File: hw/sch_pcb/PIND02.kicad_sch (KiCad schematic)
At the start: 56 parts, among them J1 Conn_Coaxial, J2 HEADER_2x05_PARALLEL, J3 HEADER_2x01, M1 HOLE M3, M2 HOLE M3, M3 HOLE, M4 HOLE, Q1 2SK2394-6, U1 OPA2314, U3 ISL21080DIH312Z-TK, U3 SHT31-DIS, U4 TPS613222ADBV

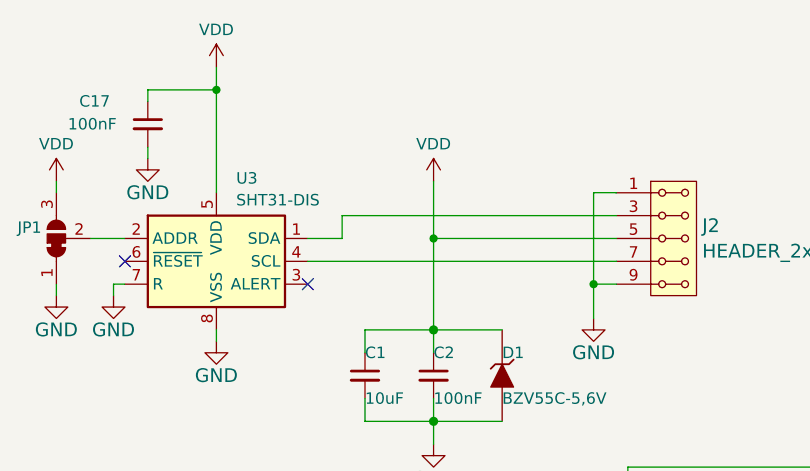
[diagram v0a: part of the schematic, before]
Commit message: Update title block Resolve ERC errors.
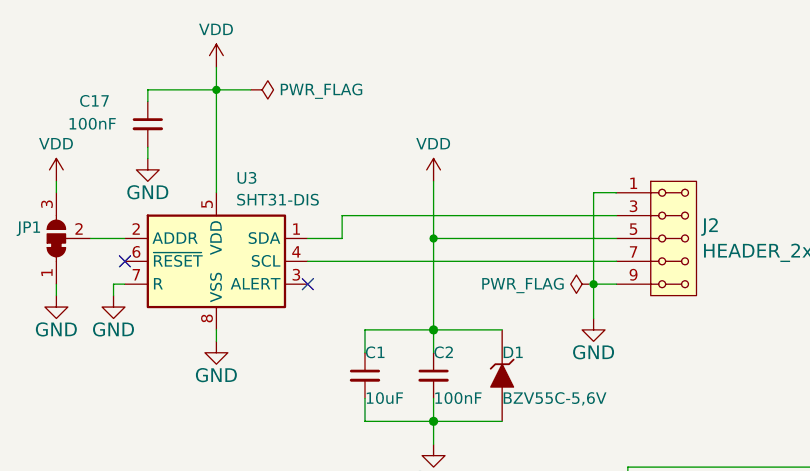
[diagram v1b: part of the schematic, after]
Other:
- company: Mlab www.mlab.cz -> kaklik@mlab.cz
- title: NAME -> PIND02A
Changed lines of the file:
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@@
   (paper "A4")
   (title_block
-    (title "NAME")
+    (title "PIND02A")
     (date "%d. %m. %Y")
-    (rev "REV")
-    (company "Mlab www.mlab.cz")
-    (comment 1 "Short description \\nTwo lines are maximum")
-    (comment 2 "nickname <email@example.com>")
+    (rev "A")
+    (company "kaklik@mlab.cz")
+    (comment 1 "PIN diode semiconductor radiation \\ndetector analogue front-end. ")
   )
   (junction (at 66.04 49.53) (diameter 1.016) (color 0 0 0 0)
@@
     (stroke (width 0) (type default))
   )
+  (wire (pts (xy 41.91 22.86) (xy 45.72 22.86))
+    (stroke (width 0) (type default))
+  )
   (wire (pts (xy 198.12 130.81) (xy 205.74 130.81))
     (stroke (width 0) (type solid))
@@
     )
   )
+  (symbol (lib_id "power:PWR_FLAG") (at 83.82 44.45 90) (unit 1)
+    (in_bom yes) (on_board yes) (dnp no) (fields_autoplaced)
+    (property "Reference" "#FLG03" (at 81.915 44.45 0)
+      (effects (font (size 1.27 1.27)) hide)
+    )
+    (property "Value" "PWR_FLAG" (at 80.6451 44.45 90)
+      (effects (font (size 1.27 1.27)) (justify left))
+    )
+    (property "Footprint" "" (at 83.82 44.45 0)
+      (effects (font (size 1.27 1.27)) hide)
+    )
+    (property "Datasheet" "~" (at 83.82 44.45 0)
+      (effects (font (size 1.27 1.27)) hide)
+    )
+    (pin "1")
+    (instances
+      (project "PIND02"
+        (path "/2ae32537-a16f-4c5b-a56b-c6dddfb8ddb4"
+          (reference "#FLG03") (unit 1)
+        )
+      )
+    )
+  )
   (symbol (lib_id "power:VDD") (at 41.91 20.32 0) (unit 1)
     (in_bom yes) (on_board yes) (dnp no) (fields_autoplaced)
@@
         )
       )
+    )
+  )
+  (symbol (lib_id "power:PWR_FLAG") (at 45.72 22.86 270) (unit 1)
+    (in_bom yes) (on_board yes) (dnp no) (fields_autoplaced)
+    (property "Reference" "#FLG02" (at 47.625 22.86 0)
+      (effects (font (size 1.27 1.27)) hide)
+    )
+    (property "Value" "PWR_FLAG" (at 48.895 22.86 90)
+      (effects (font (size 1.27 1.27)) (justify left))
+    )
+    (property "Footprint" "" (at 45.72 22.86 0)
+      (effects (font (size 1.27 1.27)) hide)
+    )
+    (property "Datasheet" "~" (at 45.72 22.86 0)
+      (effects (font (size 1.27 1.27)) hide)
+    )
+    (pin "1")
+    (instances
+      (project "PIND02"
+        (path "/2ae32537-a16f-4c5b-a56b-c6dddfb8ddb4"
+          (reference "#FLG02") (unit 1)
+        )
+      )

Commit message: Assing footprints to components. Starting of PCB design.
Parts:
- FID1, FID2: footprint (none) -> Fiducial:Fiducial_1mm_Mask2mm
- J1: footprint (none) -> Connector_Coaxial:SMA_Amphenol_901-144_Vertical; UST_ID (none) -> 5fa10cc512875025b39779f6
- J2: footprint (none) -> Mlab_Pin_Headers:Straight_2x05
- J3: footprint (none) -> Mlab_Pin_Headers:Straight_2x01
- JP1: footprint (none) -> Jumper:SolderJumper-3_P1.3mm_Bridged12_RoundedPad1.0x1.5mm
- L3: footprint (none) -> Inductor_SMD:L_0805_2012Metric; UST_ID (none) -> 626fd6fcdc56076e9a222966
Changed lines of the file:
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@@
       (effects (font (size 1.27 1.27)) (justify left))
     )
-    (property "Footprint" "" (at 24.13 39.37 0)
+    (property "Footprint" "Jumper:SolderJumper-3_P1.3mm_Bridged12_RoundedPad1.0x1.5mm" (at 24.13 39.37 0)
       (effects (font (size 1.27 1.27)) hide)
     )
     (property "Datasheet" "~" (at 24.13 39.37 0)
+      (effects (font (size 1.27 1.27)) hide)
+    )
+    (property "UST_ID" "" (at 24.13 39.37 0)
       (effects (font (size 1.27 1.27)) hide)
     )
@@
       (effects (font (size 1.27 1.27)) (justify left))
     )
-    (property "Footprint" "" (at 210.82 130.81 0)
+    (property "Footprint" "Connector_Coaxial:SMA_Amphenol_901-144_Vertical" (at 210.82 130.81 0)
       (effects (font (size 1.27 1.27)) hide)
     )
     (property "Datasheet" " ~" (at 210.82 130.81 0)
+      (effects (font (size 1.27 1.27)) hide)
+    )
+    (property "UST_ID" "5fa10cc512875025b39779f6" (at 210.82 130.81 0)
       (effects (font (size 1.27 1.27)) hide)
     )
@@
       (effects (font (size 1.524 1.524)) (justify left))
     )
-    (property "Footprint" "" (at 198.12 101.6 0)
-      (effects (font (size 1.524 1.524)))
+    (property "Footprint" "Mlab_Pin_Headers:Straight_2x01" (at 198.12 101.6 0)
+      (effects (font (size 1.524 1.524)) hide)
     )
     (property "Datasheet" "" (at 198.12 101.6 0)
       (effects (font (size 1.524 1.524)))
+    )
+    (property "UST_ID" "" (at 198.12 101.6 0)
+      (effects (font (size 1.27 1.27)) hide)
     )
     (pin "1")
@@
       (effects (font (size 1.27 1.27)) (justify left))
     )
-    (property "Footprint" "" (at 271.78 33.02 0)
+    (property "Footprint" "Fiducial:Fiducial_1mm_Mask2mm" (at 271.78 33.02 0)
       (effects (font (size 1.27 1.27)) hide)
     )
@@
       (effects (font (size 1.27 1.27)) (justify left))
     )
-    (property "Footprint" "" (at 259.08 33.02 0)
+    (property "Footprint" "Fiducial:Fiducial_1mm_Mask2mm" (at 259.08 33.02 0)
       (effects (font (size 1.27 1.27)) hide)
     )
@@
       (effects (font (size 1.27 1.27)) (justify left))
     )
-    (property "Footprint" "" (at 198.12 123.19 0)
-      (effects (font (size 1.27 1.27)) hide)
-    )
-    (property "Datasheet" "~" (at 198.12 123.19 0)
+    (property "Footprint" "Inductor_SMD:L_0805_2012Metric" (at 198.12 123.19 0)
+      (effects (font (size 1.27 1.27)) hide)
+    )
+    (property "Datasheet" "https://www.tme.eu/Document/a05ae3504cfc60ed89e3a57fb94acf5e/VIKING-NL.pdf" (at 198.12 123.19 0)
+      (effects (font (size 1.27 1.27)) hide)
+    )
+    (property "UST_ID" "626fd6fcdc56076e9a222966" (at 198.12 123.19 0)
       (effects (font (size 1.27 1.27)) hide)
     )
@@
       (effects (font (size 1.524 1.524)) (justify left))
     )
-    (property "Footprint" "" (at 92.71 34.29 0)
-      (effects (font (size 1.524 1.524)))
+    (property "Footprint" "Mlab_Pin_Headers:Straight_2x05" (at 92.71 34.29 0)
+      (effects (font (size 1.524 1.524)) hide)
     )
     (property "Datasheet" "" (at 92.71 34.29 0)

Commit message: PCB design WIP.
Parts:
- removed C11, C21, C23, C53: 10uF, Capacitor_SMD:C_0603_1608Metric, symbol Device:C
- removed C42, C50: 10uF, Capacitor_SMD:C_0603_1608Metric, symbol SPACEDOS01A_PCB01A-rescue:C-device-DATALOGGER01A-rescue-CCP2019V01A-rescue
- added C42, C50 (x5): 10uF, Capacitor_Tantalum_SMD:CP_EIA-3216-18_Kemet-A, symbol Device:C_Polarized_Small
- added M5: RFShield_TwoPieces, RF_Shielding:Laird_Technologies_BMI-S-204-F_32.00x32.00mm, symbol Device:RFShield_TwoPieces
- C10, C16, C2, C54, C59, C6: footprint Capacitor_SMD:C_0603_1608Metric -> Capacitor_SMD:C_0805_2012Metric; UST_ID 5c70984812875079b91f8bf2 -> 6508260b462c6d9e720541f1
- C15: UST_ID 628d0fc8dc56076e9a223574 -> 6508354d462c6d9e7205425e
- C24, C3, C37: footprint Capacitor_SMD:C_0603_1608Metric -> Capacitor_SMD:C_1210_3225Metric; UST_ID 643f03ef76c82a1d3b576bed -> 65082f52462c6d9e72054238
- J2: value HEADER_2x05_PARALLEL -> MLAB I2C interface
- R12: footprint Mlab_R:SMD-0805 -> Resistor_SMD:R_0805_2012Metric
- R6: footprint Resistor_SMD:R_0603_1608Metric -> Resistor_SMD:R_0805_2012Metric; UST_ID 5c70984712875079b91f8b6d -> 5c70984712875079b91f8aae
- R9: footprint Resistor_SMD:R_0603_1608Metric -> Resistor_SMD:R_0805_2012Metric; UST_ID 5c70984512875079b91f8960 -> 5c70984612875079b91f8995
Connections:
- net GND: now also C42.2, C50.2, M5.1 (Shield); no longer C2.2, C3.2, C54.2, C59.2, C59.2, C6.2, R14.2, U1.4 (V-), U3.3 (GND)
- net at C6.1, R2.1, U1.8 (V+): now also C50.1
- net at C52.1, U4.4 (VOUT): now also C42.1, C50.1
- net at R15.1, R19.2: now also C50.1
- net at C59.1, Q1.2 (D), R40.1: now also C50.1
- net at C2.1, R19.1, R22.2: now also C50.1
- new net GNDA: C2.2, C3.2, C50.2, C50.2, C50.2, C50.2, C54.2, C59.2, C59.2, C6.2, R14.2, U1.4 (V-), U3.3 (GND)

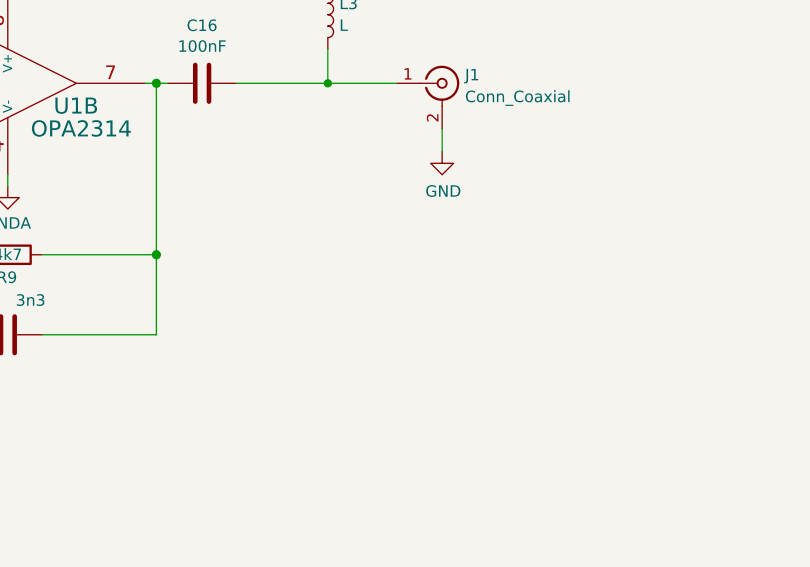
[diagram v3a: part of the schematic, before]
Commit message: The first fully routed PCB.
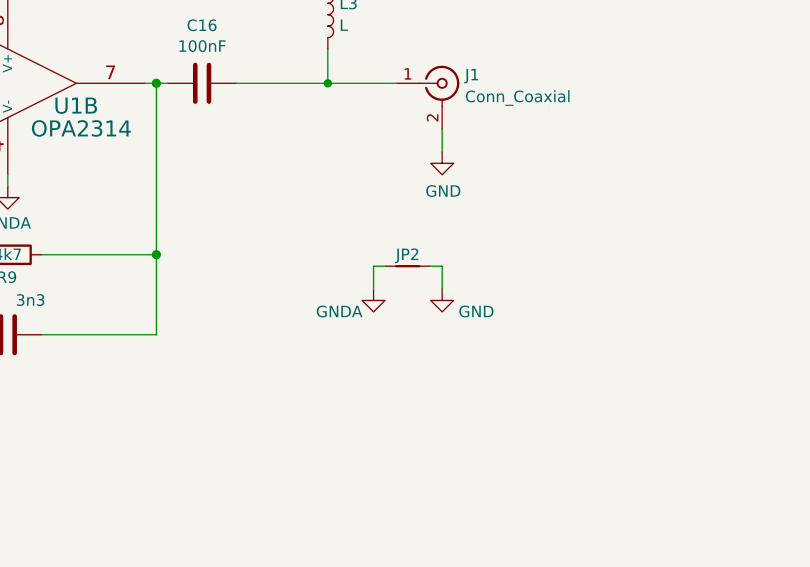
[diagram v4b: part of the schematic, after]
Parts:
- added JP2: Jumper_2_Bridged, NetTie:NetTie-2_SMD_Pad0.5mm, symbol Device:NetTie_2
- C1, C15, C32, C59: footprint Capacitor_SMD:C_0603_1608Metric -> Capacitor_SMD:C_0805_2012Metric
- R14, R15, R16, R19, R22: footprint Resistor_SMD:R_0603_1608Metric -> Resistor_SMD:R_0805_2012Metric; UST_ID 5c70984512875079b91f8960 -> 5c70984612875079b91f8995
- R2, R40: footprint Resistor_SMD:R_0603_1608Metric -> Resistor_SMD:R_0805_2012Metric; UST_ID 5c70984512875079b91f8959 -> 5c70984512875079b91f8986
- R7: footprint Resistor_SMD:R_0603_1608Metric -> Resistor_SMD:R_0805_2012Metric; UST_ID 5c70984512875079b91f8962 -> 5c70984612875079b91f899f
- R8: footprint Resistor_SMD:R_0603_1608Metric -> Resistor_SMD:R_0805_2012Metric; UST_ID 5c70984512875079b91f895c -> 5c70984512875079b91f898c
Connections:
- net GND: now also JP2.2
- net GNDA: now also JP2.1
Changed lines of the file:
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@@
     (stroke (width 0) (type default))
   )
+  (wire (pts (xy 203.2 151.13) (xy 203.2 153.67))
+    (stroke (width 0) (type default))
+  )
   (wire (pts (xy 274.32 19.05) (xy 274.32 17.78))
     (stroke (width 0) (type default))
@@
     (stroke (width 0) (type default))
   )
+  (wire (pts (xy 204.47 151.13) (xy 203.2 151.13))
+    (stroke (width 0) (type default))
+  )
   (wire (pts (xy 132.08 110.49) (xy 132.08 128.27))
     (stroke (width 0) (type solid))
@@
     (stroke (width 0) (type default))
   )
+  (wire (pts (xy 210.82 151.13) (xy 209.55 151.13))
+    (stroke (width 0) (type default))
+  )
   (wire (pts (xy 105.41 110.49) (xy 114.3 110.49))
     (stroke (width 0) (type solid))
@@
     (stroke (width 0) (type default))
   )
+  (wire (pts (xy 210.82 153.67) (xy 210.82 151.13))
+    (stroke (width 0) (type default))
+  )
   (wire (pts (xy 30.48 110.49) (xy 31.75 110.49))
     (stroke (width 0) (type solid))
@@
       (effects (font (size 1.27 1.27)))
     )
-    (property "Footprint" "Resistor_SMD:R_0603_1608Metric" (at 26.67 108.712 90)
+    (property "Footprint" "Resistor_SMD:R_0805_2012Metric" (at 26.67 108.712 90)
       (effects (font (size 1.27 1.27)) hide)
     )
@@
       (effects (font (size 1.27 1.27)) hide)
     )
-    (property "UST_ID" "5c70984512875079b91f8960" (at 26.67 110.49 0)
+    (property "UST_ID" "5c70984612875079b91f8995" (at 26.67 110.49 0)
       (effects (font (size 1.27 1.27)) hide)
     )
@@
       (effects (font (size 1.27 1.27)) (justify left))
     )
-    (property "Footprint" "Capacitor_SMD:C_0603_1608Metric" (at 160.9852 58.42 0)
+    (property "Footprint" "Capacitor_SMD:C_0805_2012Metric" (at 160.9852 58.42 0)
       (effects (font (size 1.27 1.27)) hide)
     )
@@
     )
   )
+  (symbol (lib_id "power:GNDA") (at 203.2 153.67 0) (unit 1)
+    (in_bom yes) (on_board yes) (dnp no)
+    (property "Reference" "#PWR08" (at 203.2 160.02 0)
+      (effects (font (size 1.27 1.27)) hide)
+    )
+    (property "Value" "GNDA" (at 199.39 156.21 0)
+      (effects (font (size 1.27 1.27)))
+    )
+    (property "Footprint" "" (at 203.2 153.67 0)
+      (effects (font (size 1.27 1.27)) hide)
+    )
+    (property "Datasheet" "" (at 203.2 153.67 0)
+      (effects (font (size 1.27 1.27)) hide)
+    )
+    (pin "1")
+    (instances
+      (project "PIND02"
+        (path "/2ae32537-a16f-4c5b-a56b-c6dddfb8ddb4"
+          (reference "#PWR08") (unit 1)
+        )
+      )
+      (project "PCRD07"
+        (path "/e63e39d7-6ac0-4ffd-8aa3-1841a4541b55"
+          (reference "#PWR034") (unit 1)
+        )
+      )
+    )
+  )
   (symbol (lib_id "Device:R") (at 162.56 149.86 270) (unit 1)
     (in_bom yes) (on_board yes) (dnp no)
@@
       (effects (font (size 1.27 1.27)))
     )
-    (property "Footprint" "Capacitor_SMD:C_0603_1608Metric" (at 158.75 159.7152 0)
+    (property "Footprint" "Capacitor_SMD:C_0805_2012Metric" (at 158.75 159.7152 0)
       (effects (font (size 1.27 1.27)) hide)
     )
@@
       (effects (font (size 1.27 1.27)) (justify left))
     )
-    (property "Footprint" "Capacitor_SMD:C_0603_1608Metric" (at 23.1648 172.72 0)
+    (property "Footprint" "Capacitor_SMD:C_0805_2012Metric" (at 23.1648 172.72 0)
       (effects (font (size 1.27 1.27)) hide)
     )
@@
     )
   )
+  (symbol (lib_id "Device:NetTie_2") (at 207.01 151.13 0) (unit 1)
+    (in_bom no) (on_board yes) (dnp no)
+    (property "Reference" "JP2" (at 207.01 149.86 0)
+      (effects (font (size 1.27 1.27)))
+    )
+    (property "Value" "Jumper_2_Bridged" (at 207.01 148.59 0)
+      (effects (font (size 1.27 1.27)) hide)
+    )
+    (property "Footprint" "NetTie:NetTie-2_SMD_Pad0.5mm" (at 207.01 151.13 0)
+      (effects (font (size 1.27 1.27)) hide)
+    )
+    (property "Datasheet" "~" (at 207.01 151.13 0)
+      (effects (font (size 1.27 1.27)) hide)
+    )
+    (pin "1")
+    (pin "2")
+    (instances
+      (project "PIND02"
+        (path "/2ae32537-a16f-4c5b-a56b-c6dddfb8ddb4"
+          (reference "JP2") (unit 1)
+        )
+      )
+      (project "USTTHUNDERMILLPCB01"
+        (path "/6990ffb7-4abe-4df9-bce7-87822fc68e4c"
+          (reference "JP4") (unit 1)
+        )
+      )
+      (project "PCRD07"
+        (path "/e63e39d7-6ac0-4ffd-8aa3-1841a4541b55"
+          (reference "JP1") (unit 1)
+        )
+      )
+    )
+  )
   (symbol (lib_id "MLAB_T:Q_NJFET_SDG") (at 90.17 82.55 0) (mirror y) (unit 1)
     (in_bom yes) (on_board yes) (dnp no) (fields_autoplaced)
@@
       (effects (font (size 1.27 1.27)))
     )
-    (property "Footprint" "Resistor_SMD:R_0603_1608Metric" (at 36.83 112.268 90)
+    (property "Footprint" "Resistor_SMD:R_0805_2012Metric" (at 36.83 112.268 90)
       (effects (font (size 1.27 1.27)) hide)
     )
@@
       (effects (font (size 1.27 1.27)) hide)
     )
-    (property "UST_ID" "5c70984512875079b91f8960" (at 36.83 110.49 0)
+    (property "UST_ID" "5c70984612875079b91f8995" (at 36.83 110.49 0)
       (effects (font (size 1.27 1.27)) hide)
     )
@@
       (effects (font (size 1.27 1.27)))
     )
-    (property "Footprint" "Resistor_SMD:R_0603_1608Metric" (at 63.5 112.268 90)
+    (property "Footprint" "Resistor_SMD:R_0805_2012Metric" (at 63.5 112.268 90)
       (effects (font (size 1.27 1.27)) hide)
     )
@@
       (effects (font (size 1.27 1.27)) hide)
     )
-    (property "UST_ID" "5c70984512875079b91f8960" (at 63.5 110.49 0)
+    (property "UST_ID" "5c70984612875079b91f8995" (at 63.5 110.49 0)
       (effects (font (size 1.27 1.27)) hide)
     )
@@
       (effects (font (size 1.27 1.27)))
     )
-    (property "Footprint" "Resistor_SMD:R_0603_1608Metric" (at 83.185 95.758 90)
+    (property "Footprint" "Resistor_SMD:R_0805_2012Metric" (at 83.185 95.758 90)
       (effects (font (size 1.27 1.27)) hide)
     )
@@
       (effects (font (size 1.27 1.27)) hide)
     )
-    (property "UST_ID" "5c70984512875079b91f8960" (at 83.185 97.536 0)
+    (property "UST_ID" "5c70984612875079b91f8995" (at 83.185 97.536 0)
       (effects (font (size 1.27 1.27)) hide)
     )
@@
       (effects (font (size 1.27 1.27)))
     )
-    (property "Footprint" "Resistor_SMD:R_0603_1608Metric" (at 130.81 62.992 90)
+    (property "Footprint" "Resistor_SMD:R_0805_2012Metric" (at 130.81 62.992 90)
       (effects (font (size 1.27 1.27)) hide)
     )
@@
       (effects (font (size 1.27 1.27)) hide)
     )
-    (property "UST_ID" "5c70984512875079b91f8959" (at 130.81 64.77 0)
+    (property "UST_ID" "5c70984512875079b91f8986" (at 130.81 64.77 0)
       (effects (font (size 1.27 1.27)) hide)
     )
@@
       (effects (font (size 1.27 1.27)))
     )
-    (property "Footprint" "Resistor_SMD:R_0603_1608Metric" (at 160.782 90.17 90)
+    (property "Footprint" "Resistor_SMD:R_0805_2012Metric" (at 160.782 90.17 90)
       (effects (font (size 1.27 1.27)) hide)
     )
@@
       (effects (font (size 1.27 1.27)) hide)
     )
-    (property "UST_ID" "5c70984512875079b91f8959" (at 162.56 90.17 0)
+    (property "UST_ID" "5c70984512875079b91f8986" (at 162.56 90.17 0)
       (effects (font (size 1.27 1.27)) hide)
     )
@@
       (effects (font (size 1.27 1.27)) (justify left))
     )
-    (property "Footprint" "Capacitor_SMD:C_0603_1608Metric" (at 172.4152 58.42 0)
+    (property "Footprint" "Capacitor_SMD:C_0805_2012Metric" (at 172.4152 58.42 0)
       (effects (font (size 1.27 1.27)) hide)
     )
@@
       (effects (font (size 1.27 1.27)) (justify right))
     )
-    (property "Footprint" "Resistor_SMD:R_0603_1608Metric" (at 144.018 133.35 90)
+    (property "Footprint" "Resistor_SMD:R_0805_2012Metric" (at 144.018 133.35 90)
       (effects (font (size 1.27 1.27)) hide)
     )
@@
       (effects (font (size 1.27 1.27)) hide)
     )
-    (property "UST_ID" "5c70984512875079b91f8962" (at 142.24 133.35 0)
+    (property "UST_ID" "5c70984612875079b91f899f" (at 142.24 133.35 0)
       (effects (font (size 1.27 1.27)) hide)
     )
@@
       (effects (font (size 1.27 1.27)))
     )
-    (property "Footprint" "Resistor_SMD:R_0603_1608Metric" (at 149.352 163.83 90)
+    (property "Footprint" "Resistor_SMD:R_0805_2012Metric" (at 149.352 163.83 90)
       (effects (font (size 1.27 1.27)) hide)
     )
@@
       (effects (font (size 1.27 1.27)) hide)
     )
-    (property "UST_ID" "5c70984512875079b91f895c" (at 151.13 163.83 0)
+    (property "UST_ID" "5c70984512875079b91f898c" (at 151.13 163.83 0)
       (effects (font (size 1.27 1.27)) hide)
     )
@@
       (effects (font (size 1.27 1.27)))
     )
-    (property "Footprint" "Resistor_SMD:R_0603_1608Metric" (at 82.55 108.712 90)
+    (property "Footprint" "Resistor_SMD:R_0805_2012Metric" (at 82.55 108.712 90)
       (effects (font (size 1.27 1.27)) hide)
     )
@@
       (effects (font (size 1.27 1.27)) hide)
     )
-    (property "UST_ID" "5c70984512875079b91f8960" (at 82.55 110.49 0)
+    (property "UST_ID" "5c70984612875079b91f8995" (at 82.55 110.49 0)
       (effects (font (size 1.27 1.27)) hide)
     )
@@
         )
       )
+    )
+  )
+  (symbol (lib_id "power:GND") (at 210.82 153.67 0) (unit 1)
+    (in_bom yes) (on_board yes) (dnp no)
+    (property "Reference" "#PWR09" (at 210.82 160.02 0)
+      (effects (font (size 1.27 1.27)) hide)
+    )
+    (property "Value" "GND" (at 214.63 156.21 0)
+      (effects (font (size 1.27 1.27)))
+    )
+    (property "Footprint" "" (at 210.82 153.67 0)
+      (effects (font (size 1.27 1.27)) hide)
+    )
+    (property "Datasheet" "" (at 210.82 153.67 0)
+      (effects (font (size 1.27 1.27)) hide)
+    )
+    (pin "1")
+    (instances
+      (project "PIND02"
+        (path "/2ae32537-a16f-4c5b-a56b-c6dddfb8ddb4"
+          (reference "#PWR09") (unit 1)
+        )
+      )
+      (project "PCRD07"
+        (path "/e63e39d7-6ac0-4ffd-8aa3-1841a4541b55"
+          (reference "#PWR035") (unit 1)
+        )
+      )
